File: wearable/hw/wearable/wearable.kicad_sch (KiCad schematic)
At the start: 125 parts, among them IC1 LM4041CILPR, J2 Conn_02x05_Odd_Even, J8 USBC Charger, SW1 SW_Toggle, U1 LT3042xMSE, U2 BNO080, U3 nRF54L15-QFXX, U4 TPS61040DBV, U5 ADS1299IPAG, U6 nPM1300-QEXX, Y1 32MHz, Y2 32.768kHz, Y3 32.768kHz

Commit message: Ready for review
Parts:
- removed TP20: TP, TestPoint:TestPoint_THTPad_D1.0mm_Drill0.5mm, symbol RSLK2:Testpoint_1
- added R16: 10k, Resistor_SMD:R_0402_1005Metric, symbol Device:R_US
- C32: renamed from C54; footprint Capacitor_SMD:C_0402_1005Metric -> Capacitor_SMD:C_0201_0603Metric
- C36: renamed from C55; footprint Capacitor_SMD:C_0402_1005Metric -> Capacitor_SMD:C_0201_0603Metric
- C38: renamed from C56; footprint Capacitor_SMD:C_0402_1005Metric -> Capacitor_SMD:C_0201_0603Metric
- L2: renamed from L5; footprint Inductor_SMD:L_0402_1005Metric_Pad0.77x0.64mm_HandSolder -> Inductor_SMD:L_0201_0603Metric
- L3: renamed from L6; footprint Inductor_SMD:L_0402_1005Metric_Pad0.77x0.64mm_HandSolder -> Inductor_SMD:L_0201_0603Metric
- L4: renamed from L7; footprint Inductor_SMD:L_0402_1005Metric_Pad0.77x0.64mm_HandSolder -> Inductor_SMD:L_0201_0603Metric
- SW1: footprint Connector_PinHeader_1.00mm:PinHeader_1x02_P1.00mm_Vertical -> Connector_PinHeader_1.27mm:PinHeader_1x02_P1.27mm_Vertical
- renumbered C10 to C1, C27 to C10, C2 to C11, C3 to C12, C7 to C13, C9 to C14, C1 to C15, C58 to C16, C57 to C17, C37 to C18, C48 to C19, C12 to C2, C47 to C20, C49 to C21, C51 to C22, C45 to C23, C50 to C24, C46 to C25, C60 to C26, C53 to C27, C16 to C28, C19 to C29, C30 to C3, C23 to C30, C52 to C31, C21 to C33, C18 to C34, C14 to C35, C15 to C37, C13 to C39, C29 to C4, C24 to C40, C20 to C41, C25 to C42, C17 to C43, C11 to C44, C33 to C45, C32 to C46, C31 to C47, C36 to C48, C26 to C49, C4 to C5, C5 to C6, C8 to C7, C6 to C8, C28 to C9, D4 to D1, D1 to D2, D2 to D3, J8 to J1, L2 to L1, L3 to L5, L4 to L6, L1 to L7, R20 to R1, R15 to R10, R22 to R11, R18 to R12, R19 to R13, R5 to R14, R6 to R15, R24 to R17, R25 to R18, R27 to R19, R4 to R2, R26 to R20, R7 to R21, R10 to R22, R9 to R23, R3 to R24, R17 to R25, R11 to R26, R16 to R27, R21 to R3, R23 to R4, R2 to R5, R1 to R6, R12 to R7, R13 to R8, R14 to R9, TP2 to TP1, TP8 to TP10, TP13 to TP11, TP10 to TP12, TP3 to TP13, TP12 to TP14, TP4 to TP15, TP1 to TP2, TP5 to TP3, TP6 to TP4, TP21 to TP5, TP9 to TP6, TP11 to TP8, TP14 to TP9, U5 to U1, U3 to U2, U2 to U3, U6 to U4, U1 to U5, U4 to U6, Y2 to Y1, Y3 to Y2, Y1 to Y3
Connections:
- net CC1 is gone; now on an unnamed net: U4.23 (CC1)
- net CC2 is gone; now on an unnamed net: U4.24 (CC2)
- net GND: now also R17.2, R18.2, R16.2
- net at SW1.2: now also U4.15 (SHPHLD); no longer U4.18 (NTC)
- net SHPHLD: no longer names the net of U2.23 (P0.00)
- net SHPHLD: no longer U4.15 (SHPHLD)
- new net: R16.1, U4.18 (NTC)
- no-connect marks 33 -> 31
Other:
- moved on the sheet: SW1

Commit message: Gerbers
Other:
- note removed: "TODO: integrate nordic pmic and find good boost converter to use with the LT LDO"
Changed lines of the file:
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@@
-		)
-	)
-	(text "TODO: integrate nordic pmic and find good boost converter to use with the LT LDO"
-		(exclude_from_sim no)
-		(at 67.056 303.022 0)
-		(effects
-			(font
-				(size 1.27 1.27)
-			)
 		)
 	)

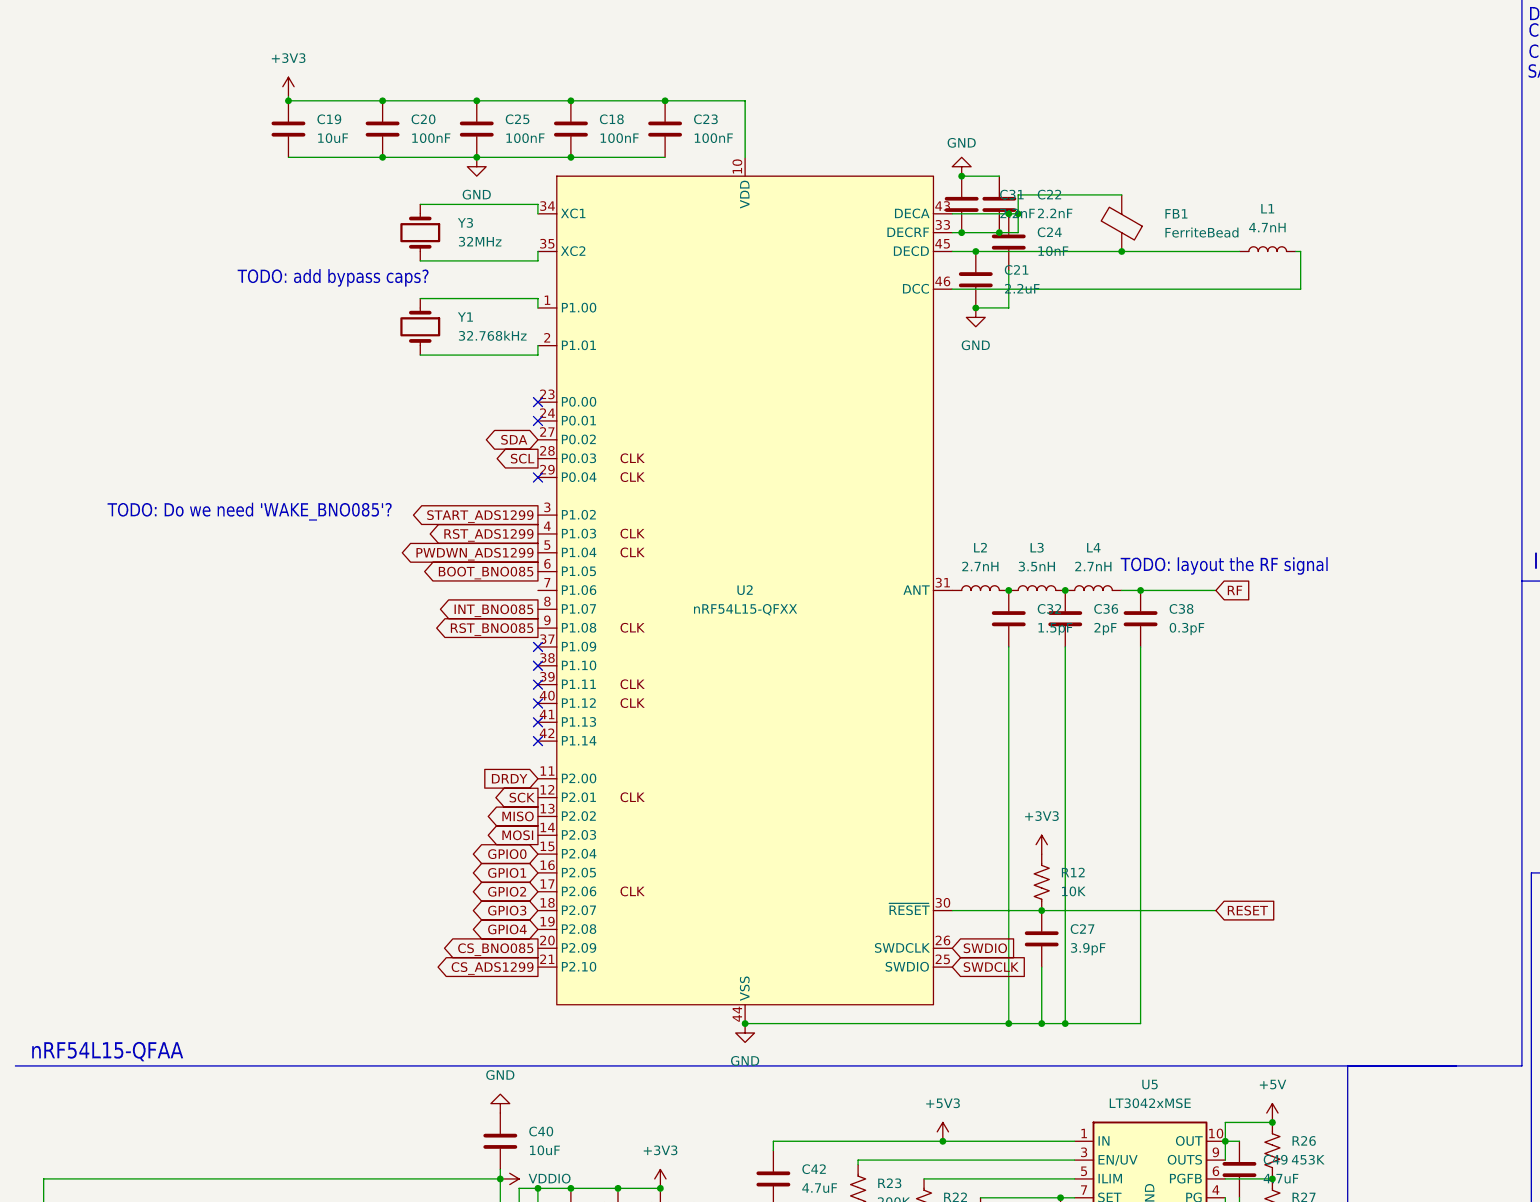
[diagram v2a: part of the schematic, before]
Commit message: BL54L15 added
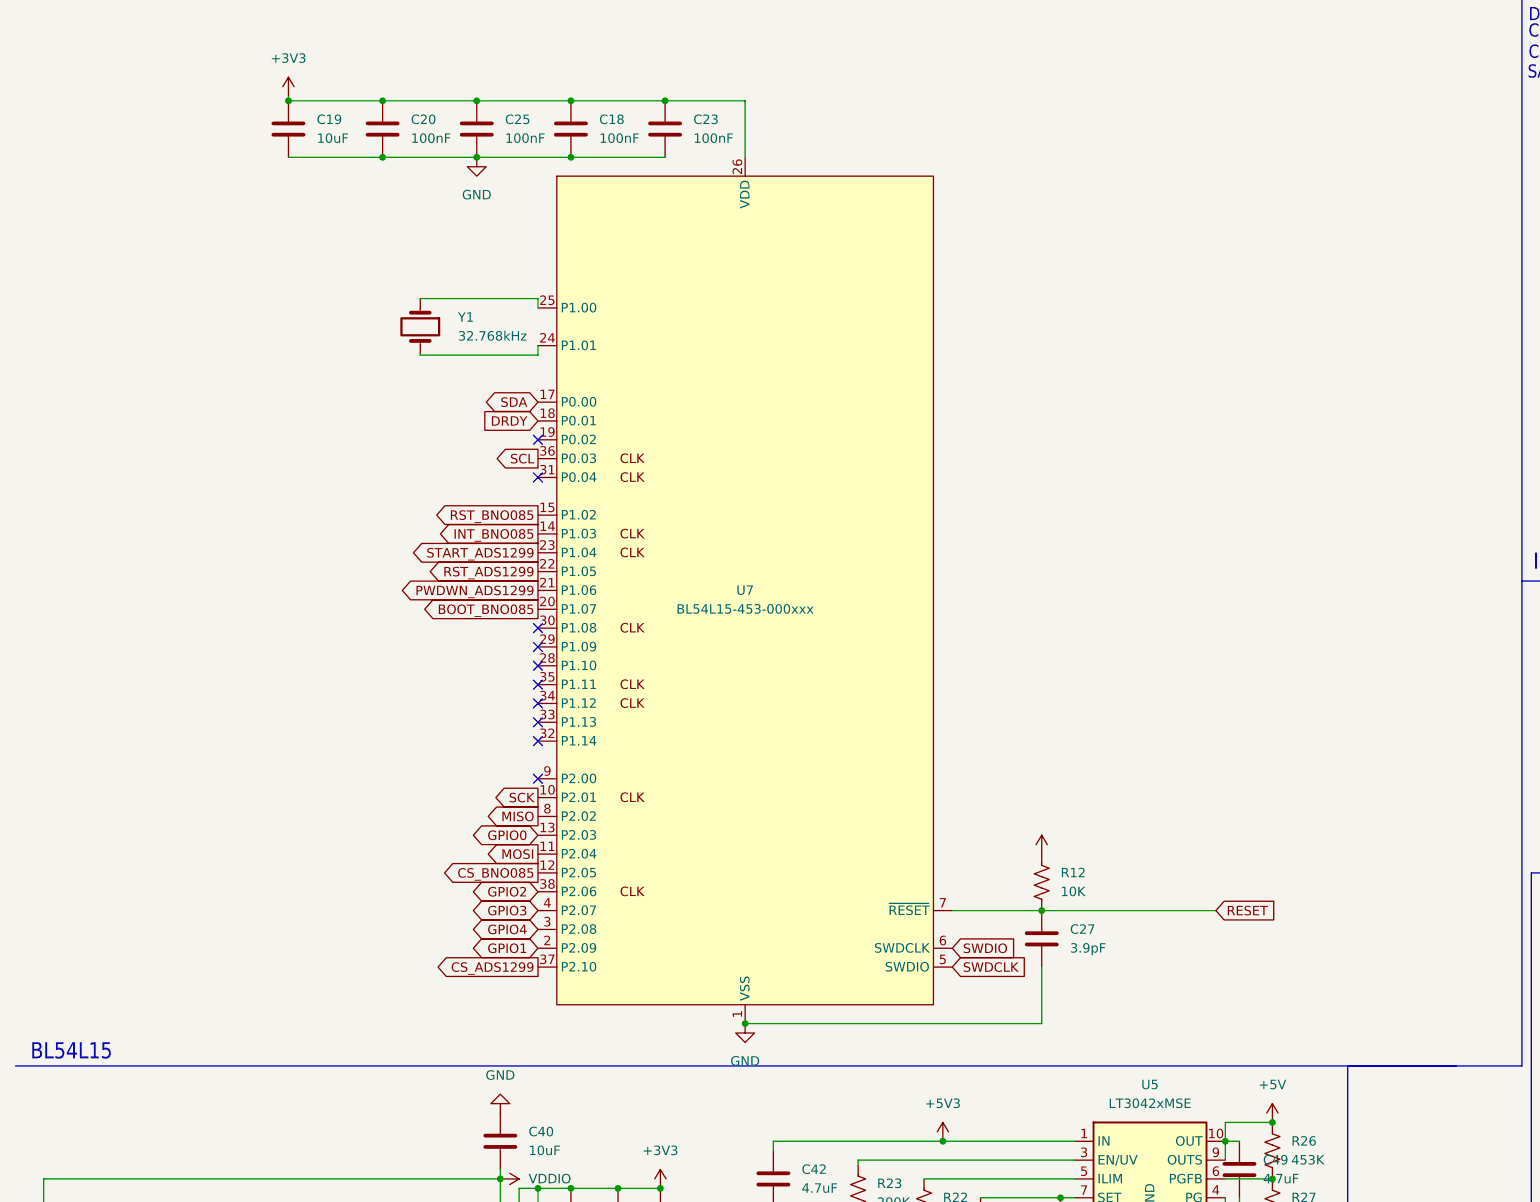
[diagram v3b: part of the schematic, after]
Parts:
- removed C21: 2.2uF, Capacitor_SMD:C_0402_1005Metric, symbol ECE445L:C
- removed C22, C31: 2.2nF, Capacitor_SMD:C_0402_1005Metric, symbol ECE445L:C
- removed C24: 10nF, Capacitor_SMD:C_0402_1005Metric, symbol ECE445L:C
- removed C32: 1.5pF, Capacitor_SMD:C_0201_0603Metric, symbol ECE445L:C
- removed C36: 2pF, Capacitor_SMD:C_0201_0603Metric, symbol ECE445L:C
- removed C38: 0.3pF, Capacitor_SMD:C_0201_0603Metric, symbol ECE445L:C
- removed FB1: FerriteBead, Inductor_SMD:L_0402_1005Metric_Pad0.77x0.64mm_HandSolder, symbol Device:FerriteBead
- removed L1: 4.7nH, Inductor_SMD:L_0603_1608Metric, symbol Device:L
- removed L2, L4: 2.7nH, Inductor_SMD:L_0201_0603Metric, symbol Device:L
- removed L3: 3.5nH, Inductor_SMD:L_0201_0603Metric, symbol Device:L
- removed U2: nRF54L15-QFXX, Package_DFN_QFN:QFN-48-1EP_6x6mm_P0.4mm_EP4.6x4.6mm, symbol PCM_nordic-lib-kicad-nrf54l:nRF54L15-QFXX
- removed Y3: 32MHz, Unknown:Crystal_SMD_2016-2Pin_2.0x1.6mm, symbol Device:Crystal
- added U7: BL54L15-453-000xxx, PCM_nordic-lib-kicad-nrf54-modules:BL54Lxx-LGA-39_14x10mm, symbol PCM_nordic-lib-kicad-nrf54-modules:BL54L15-453-000xxx
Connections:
- net +3V3: now also U7.26 (VDD)
- net BOOT_BNO085: now also U7.20 (P1.07)
- net CS_ADS1299: now also U7.37 (P2.10)
- net CS_BNO085: now also U7.12 (P2.05)
- net DRDY: now also U7.18 (P0.01)
- net GND: now also U7.1 (VSS), U7.16 (VSS), U7.27 (VSS), U7.39 (VSS)
- net GPIO0: now also U7.13 (P2.03)
- net GPIO1: now also U7.2 (P2.09)
- net GPIO2: now also U7.38 (P2.06)
- net GPIO3: now also U7.4 (P2.07)
- net GPIO4: now also U7.3 (P2.08)
- net INT_BNO085: now also U7.14 (P1.03)
- net MISO: now also U7.8 (P2.02)
- net MOSI: now also U7.11 (P2.04)
- net PWDWN_ADS1299: now also U7.21 (P1.06)
- net RESET: now also U7.7 (~{RESET})
- net RST_ADS1299: now also U7.22 (P1.05)
- net RST_BNO085: now also U7.15 (P1.02)
- net SCK: now also U7.10 (P2.01)
- net SCL: now also U7.36 (P0.03)
- net SDA: now also U7.17 (P0.00)
- net START_ADS1299: now also U7.23 (P1.04)
- net SWDCLK: now also U7.5 (SWDIO)
- net SWDIO: now also U7.6 (SWDCLK)
- net at Y1.1: now also U7.25 (P1.00)
- net at Y1.2: now also U7.24 (P1.01)
- no-connect marks 31 -> 32
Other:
- note added: "BL54L15"
- note removed: "TODO: Do we need 'WAKE_BNO085'?"
- note removed: "TODO: add bypass caps?"
- note removed: "TODO: layout the RF signal"
- note removed: "nRF54L15-QFAA"

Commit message: Checking with Alex
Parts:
- removed C18, C20, C23, C25: 100nF, Capacitor_SMD:C_0402_1005Metric, symbol ECE445L:C
- removed C19, C28, C29, C30, C34, C37: 10uF, Capacitor_SMD:C_0402_1005Metric, symbol ECE445L:C
- removed J1: USBC Charger, Connector_PinHeader_2.54mm:PinHeader_1x08_P2.54mm_Vertical, symbol ECE445L:Conn_01x08_Pin
- removed L6: 2.2uH, Inductor_SMD:L_0402_1005Metric_Pad0.77x0.64mm_HandSolder, symbol Device:L
- removed R18: 150k, Resistor_SMD:R_0402_1005Metric, symbol Device:R_US
- added C21: 1uF, Capacitor_SMD:C_0402_1005Metric, symbol ECE445L:C
- added J1: USB_C_Receptacle_PowerOnly_6P, Connector_PinHeader_2.54mm:PinHeader_1x08_P2.54mm_Vertical, symbol Connector:USB_C_Receptacle_PowerOnly_6P
- R17: value 47k -> 250k
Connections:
- net VDDIO is gone; now on net +3V3: C40.2, R19.1, R20.1, U4.12 (VDDIO)
- net VINLDO1 is gone; now on net GND: U4.28 (LSIN1/VINLDO1)
- net VINLDO2 is gone; now on net +3V3: U4.30 (LSIN2/VINLDO2)
- net +3V3: now also C35.1, L5.1, U4.32 (VOUT2); no longer C45.1, C46.1, C47.1, U4.20 (VSYS), U4.4 (PVDD)
- net +5V3: now also R23.1, U5.3 (EN/UV)
- net +5V_USB: now also J1.A9 (VBUS), J1.B9 (VBUS)
- net GND: now also C35.2, U4.17 (VSET1), U4.2 (PVSS1), U4.29 (LSOUT1/VOUTLDO1), U4.6 (PVSS2), C21.2, J1.A12 (GND), J1.B12 (GND), J1.S1 (SHIELD)
- net at R17.1: now also U4.16 (VSET2); no longer U4.17 (VSET1)
- net at U4.5 (SW2): now also L5.2
- net at U4.31 (LSOUT2/VOUTLDO2): now also C21.1
- net at U4.3 (SW1): no longer L5.2
- net at U4.23 (CC1): now also J1.A5 (CC1)
- net at U4.24 (CC2): now also J1.B5 (CC2)
- new net VSYS: C45.1, C46.1, C47.1, U4.1 (VOUT1), U4.20 (VSYS), U4.4 (PVDD)
- no-connect marks 32 -> 28
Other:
- moved on the sheet: BT1, C33, C35, C39, C40, C44, C45, C46, C47, L5, R16, R17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

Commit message: Almost done with design review...
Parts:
- removed C47: 10uF, Capacitor_SMD:C_0402_1005Metric, symbol ECE445L:C
- removed J1: USB_C_Receptacle_PowerOnly_6P, Connector_PinHeader_2.54mm:PinHeader_1x08_P2.54mm_Vertical, symbol Connector:USB_C_Receptacle_PowerOnly_6P
- added J3: USB-C Connector, Connector_PinHeader_2.54mm:PinHeader_1x08_P2.54mm_Vertical, symbol ECE445L:Conn_01x08_Pin
- added R18: 10K, Resistor_SMD:R_0402_1005Metric, symbol Device:R_US
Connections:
- net +5V_USB: now also J3.2 (Pin_2)
- net GND: now also U4.24 (CC2), J3.1 (Pin_1), J3.3 (Pin_3), J3.7 (Pin_7), J3.8 (Pin_8)
- net at C3.1, R5.1, U1.62 (BIASIN)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: now also R18.2; no longer E5.1
- net at U4.23 (CC1): now also J3.4 (Pin_4)
- new net: E5.1, R18.1
- no-connect marks 28 -> 30
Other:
- moved on the sheet: C45, C46, C49, E5

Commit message: Design review DONE
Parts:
- removed IC1: LM4041CILPR, ECE445L:ti_LM4041CILPR, symbol ti_LM4041CILPR:LM4041CILPR
- removed R6: 5.1K, Resistor_SMD:R_0402_1005Metric, symbol Device:R_US

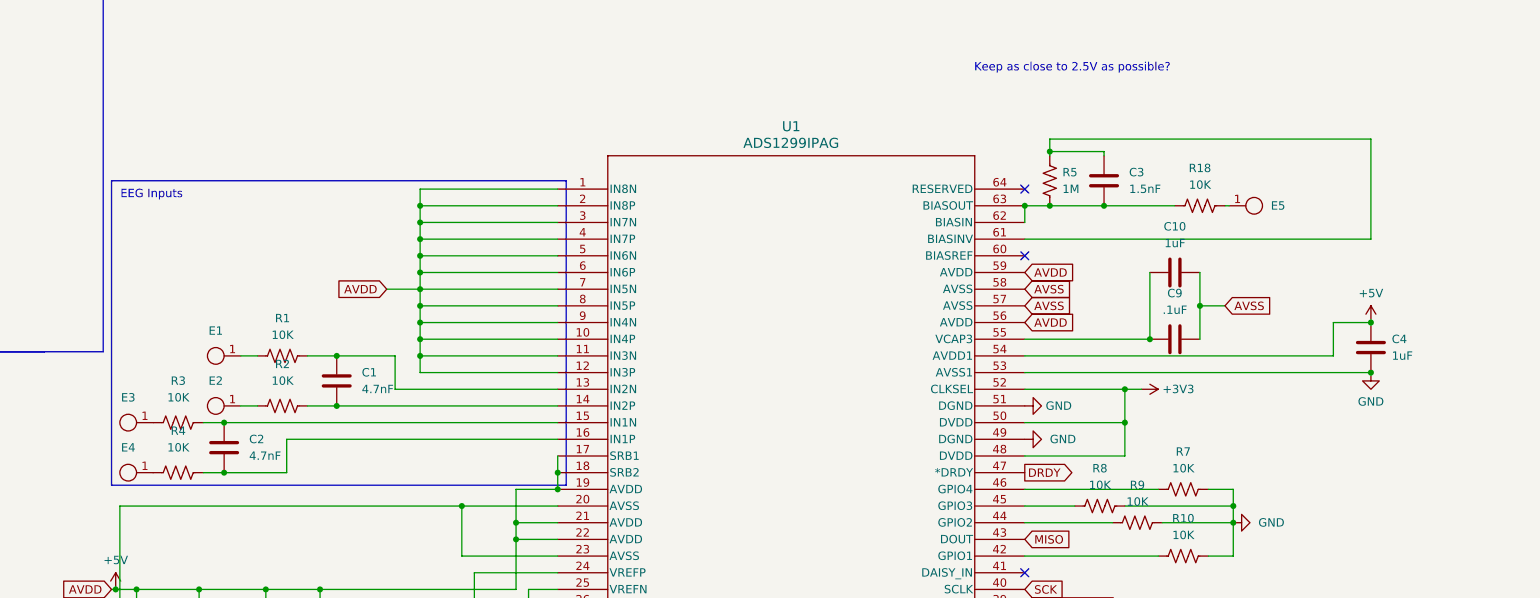
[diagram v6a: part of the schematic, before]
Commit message: ESD protection, cyton reference, silkscreen update
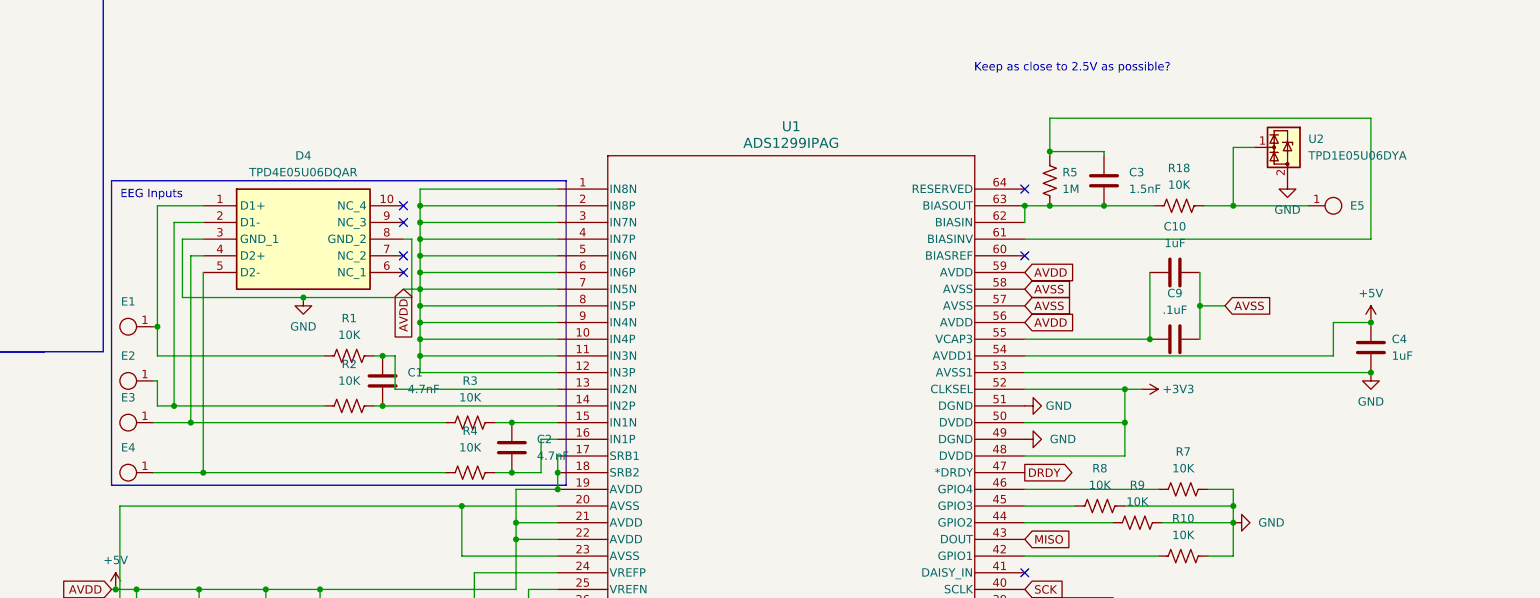
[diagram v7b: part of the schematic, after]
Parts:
- added D4: TPD4E05U06DQAR, DQA(R-PUSON-N10), symbol TPD4E05U06DQAR:TPD4E05U06DQAR
- added U2: TPD1E05U06DYA, Diode_SMD:D_SOD-523, symbol Power_Protection:TPD1E05U06DYA
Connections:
- net GND: now also D4.3 (GND_1), D4.8 (GND_2), U2.2 (GND)
- net at E3.1, R3.2: now also D4.4 (D2+)
- net at E2.1, R2.2: now also D4.2 (D1-)
- net at E4.1, R4.2: now also D4.5 (D2-)
- net at E1.1, R1.2: now also D4.1 (D1+)
- net at E5.1, R18.1: now also U2.1 (I/O)
- no-connect marks 30 -> 34
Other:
- moved on the sheet: C1, C2, E1, E2, E5, R1, R18, R2, R3, R4
